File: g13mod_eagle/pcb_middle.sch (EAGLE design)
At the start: 65 parts

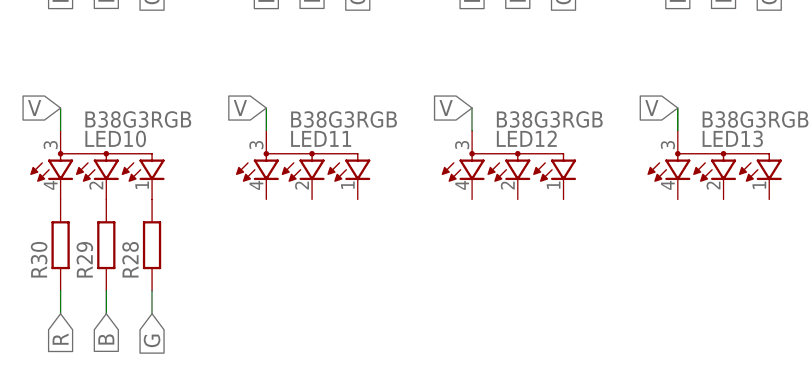
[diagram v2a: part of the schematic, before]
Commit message: wiring middle pcb
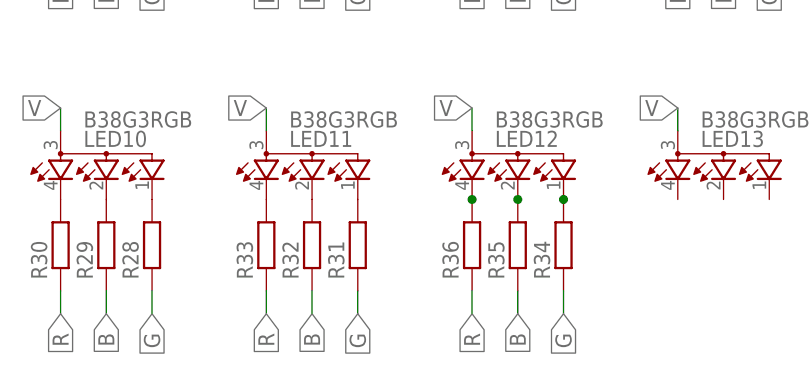
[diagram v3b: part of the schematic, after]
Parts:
- added R31, R32, R33, R34, R35, R36: (no value), rcl:R-EU_R0603
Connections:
- new net N$31: LED11.CGREEN, R31.2
- new net N$32: LED11.CBLUE, R32.2
- new net N$33: LED11.CRED, R33.2
- new net N$34: LED12.CGREEN, R34.2
- new net N$35: LED12.CBLUE, R35.2
- new net N$36: LED12.CRED, R36.2
- net B: now also R32.1, R35.1
- net G: now also R31.1, R34.1
- net R: now also R33.1, R36.1
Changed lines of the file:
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@@
 <part name="R29" library="rcl" library_urn="urn:adsk.eagle:library:334" deviceset="R-EU_" device="R0603" package3d_urn="urn:adsk.eagle:package:23555/3"/>
 <part name="R30" library="rcl" library_urn="urn:adsk.eagle:library:334" deviceset="R-EU_" device="R0603" package3d_urn="urn:adsk.eagle:package:23555/3"/>
+<part name="R31" library="rcl" library_urn="urn:adsk.eagle:library:334" deviceset="R-EU_" device="R0603" package3d_urn="urn:adsk.eagle:package:23555/3"/>
+<part name="R32" library="rcl" library_urn="urn:adsk.eagle:library:334" deviceset="R-EU_" device="R0603" package3d_urn="urn:adsk.eagle:package:23555/3"/>
+<part name="R33" library="rcl" library_urn="urn:adsk.eagle:library:334" deviceset="R-EU_" device="R0603" package3d_urn="urn:adsk.eagle:package:23555/3"/>
+<part name="R34" library="rcl" library_urn="urn:adsk.eagle:library:334" deviceset="R-EU_" device="R0603" package3d_urn="urn:adsk.eagle:package:23555/3"/>
+<part name="R35" library="rcl" library_urn="urn:adsk.eagle:library:334" deviceset="R-EU_" device="R0603" package3d_urn="urn:adsk.eagle:package:23555/3"/>
+<part name="R36" library="rcl" library_urn="urn:adsk.eagle:library:334" deviceset="R-EU_" device="R0603" package3d_urn="urn:adsk.eagle:package:23555/3"/>
 </parts>
 <sheets>
@@
 <attribute name="VALUE" x="66.802" y="-125.73" size="1.778" layer="96" rot="R90"/>
 </instance>
+<instance part="R31" gate="G$1" x="96.52" y="-121.92" smashed="yes" rot="R90">
+<attribute name="NAME" x="95.0214" y="-125.73" size="1.778" layer="95" rot="R90"/>
+<attribute name="VALUE" x="99.822" y="-125.73" size="1.778" layer="96" rot="R90"/>
+</instance>
+<instance part="R32" gate="G$1" x="91.44" y="-121.92" smashed="yes" rot="R90">
+<attribute name="NAME" x="89.9414" y="-125.73" size="1.778" layer="95" rot="R90"/>
+<attribute name="VALUE" x="94.742" y="-125.73" size="1.778" layer="96" rot="R90"/>
+</instance>
+<instance part="R33" gate="G$1" x="86.36" y="-121.92" smashed="yes" rot="R90">
+<attribute name="NAME" x="84.8614" y="-125.73" size="1.778" layer="95" rot="R90"/>
+<attribute name="VALUE" x="89.662" y="-125.73" size="1.778" layer="96" rot="R90"/>
+</instance>
+<instance part="R34" gate="G$1" x="119.38" y="-121.92" smashed="yes" rot="R90">
+<attribute name="NAME" x="117.8814" y="-125.73" size="1.778" layer="95" rot="R90"/>
+<attribute name="VALUE" x="122.682" y="-125.73" size="1.778" layer="96" rot="R90"/>
+</instance>
+<instance part="R35" gate="G$1" x="114.3" y="-121.92" smashed="yes" rot="R90">
+<attribute name="NAME" x="112.8014" y="-125.73" size="1.778" layer="95" rot="R90"/>
+<attribute name="VALUE" x="117.602" y="-125.73" size="1.778" layer="96" rot="R90"/>
+</instance>
+<instance part="R36" gate="G$1" x="109.22" y="-121.92" smashed="yes" rot="R90">
+<attribute name="NAME" x="107.7214" y="-125.73" size="1.778" layer="95" rot="R90"/>
+<attribute name="VALUE" x="112.522" y="-125.73" size="1.778" layer="96" rot="R90"/>
+</instance>
 </instances>
 <busses>
@@
 <label x="68.58" y="-129.54" size="1.778" layer="95" rot="R270" xref="yes"/>
 </segment>
+<segment>
+<pinref part="R32" gate="G$1" pin="1"/>
+<wire x1="91.44" y1="-127" x2="91.44" y2="-129.54" width="0.1524" layer="91"/>
+<label x="91.44" y="-129.54" size="1.778" layer="95" rot="R270" xref="yes"/>
+</segment>
+<segment>
+<pinref part="R35" gate="G$1" pin="1"/>
+<wire x1="114.3" y1="-127" x2="114.3" y2="-129.54" width="0.1524" layer="91"/>
+<label x="114.3" y="-129.54" size="1.778" layer="95" rot="R270" xref="yes"/>
+</segment>
 </net>
 <net name="R" class="0">
@@
 <label x="63.5" y="-129.54" size="1.778" layer="95" rot="R270" xref="yes"/>
 </segment>
+<segment>
+<pinref part="R33" gate="G$1" pin="1"/>
+<wire x1="86.36" y1="-127" x2="86.36" y2="-129.54" width="0.1524" layer="91"/>
+<label x="86.36" y="-129.54" size="1.778" layer="95" rot="R270" xref="yes"/>
+</segment>
+<segment>
+<pinref part="R36" gate="G$1" pin="1"/>
+<wire x1="109.22" y1="-127" x2="109.22" y2="-129.54" width="0.1524" layer="91"/>
+<label x="109.22" y="-129.54" size="1.778" layer="95" rot="R270" xref="yes"/>
+</segment>
 </net>
 <net name="G" class="0">
@@
 <wire x1="73.66" y1="-127" x2="73.66" y2="-129.54" width="0.1524" layer="91"/>
 <label x="73.66" y="-129.54" size="1.778" layer="95" rot="R270" xref="yes"/>
+</segment>
+<segment>
+<pinref part="R31" gate="G$1" pin="1"/>
+<wire x1="96.52" y1="-127" x2="96.52" y2="-129.54" width="0.1524" layer="91"/>
+<label x="96.52" y="-129.54" size="1.778" layer="95" rot="R270" xref="yes"/>
+</segment>
+<segment>
+<pinref part="R34" gate="G$1" pin="1"/>
+<wire x1="119.38" y1="-127" x2="119.38" y2="-129.54" width="0.1524" layer="91"/>
+<label x="119.38" y="-129.54" size="1.778" layer="95" rot="R270" xref="yes"/>
 </segment>
 </net>
@@
 </segment>
 </net>
+<net name="N$31" class="0">
+<segment>
+<pinref part="R31" gate="G$1" pin="2"/>
+<pinref part="LED11" gate="G$1" pin="CGREEN"/>
+</segment>
+</net>
+<net name="N$32" class="0">
+<segment>
+<pinref part="R32" gate="G$1" pin="2"/>
+<pinref part="LED11" gate="G$1" pin="CBLUE"/>
+</segment>
+</net>
+<net name="N$33" class="0">
+<segment>
+<pinref part="R33" gate="G$1" pin="2"/>
+<pinref part="LED11" gate="G$1" pin="CRED"/>
+</segment>
+</net>
+<net name="N$34" class="0">
+<segment>
+<pinref part="R34" gate="G$1" pin="2"/>
+<junction x="119.38" y="-116.84"/>
+<pinref part="LED12" gate="G$1" pin="CGREEN"/>
+</segment>
+</net>
+<net name="N$35" class="0">
+<segment>
+<pinref part="R35" gate="G$1" pin="2"/>
+<junction x="114.3" y="-116.84"/>
+<pinref part="LED12" gate="G$1" pin="CBLUE"/>
+</segment>
+</net>
+<net name="N$36" class="0">
+<segment>
+<pinref part="R36" gate="G$1" pin="2"/>
+<junction x="109.22" y="-116.84"/>
+<pinref part="LED12" gate="G$1" pin="CRED"/>
+</segment>
+</net>

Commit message: wiring middle pcb
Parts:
- added R37, R38, R39, R40, R41, R42, R43, R44, R45: (no value), rcl:R-EU_R0603
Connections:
- new net N$37: LED13.CGREEN, R37.2
- new net N$38: LED13.CBLUE, R38.2
- new net N$39: LED13.CRED, R39.2
- new net N$40: LED14.CGREEN, R40.2
- new net N$41: LED14.CBLUE, R41.2
- new net N$42: LED14.CRED, R42.2
- new net N$43: D1.BLUE_CATHODE, R43.2
- new net N$44: D1.GREEN_CATHODE, R44.2
- new net N$45: D1.RED_CATHODE, R45.2
- net B: now also R38.1, R41.1, R44.1
- net G: now also R37.1, R40.1, R43.1
- net R: now also R39.1, R42.1, R45.1
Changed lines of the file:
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@@
 <part name="R35" library="rcl" library_urn="urn:adsk.eagle:library:334" deviceset="R-EU_" device="R0603" package3d_urn="urn:adsk.eagle:package:23555/3"/>
 <part name="R36" library="rcl" library_urn="urn:adsk.eagle:library:334" deviceset="R-EU_" device="R0603" package3d_urn="urn:adsk.eagle:package:23555/3"/>
+<part name="R37" library="rcl" library_urn="urn:adsk.eagle:library:334" deviceset="R-EU_" device="R0603" package3d_urn="urn:adsk.eagle:package:23555/3"/>
+<part name="R38" library="rcl" library_urn="urn:adsk.eagle:library:334" deviceset="R-EU_" device="R0603" package3d_urn="urn:adsk.eagle:package:23555/3"/>
+<part name="R39" library="rcl" library_urn="urn:adsk.eagle:library:334" deviceset="R-EU_" device="R0603" package3d_urn="urn:adsk.eagle:package:23555/3"/>
+<part name="R40" library="rcl" library_urn="urn:adsk.eagle:library:334" deviceset="R-EU_" device="R0603" package3d_urn="urn:adsk.eagle:package:23555/3"/>
+<part name="R41" library="rcl" library_urn="urn:adsk.eagle:library:334" deviceset="R-EU_" device="R0603" package3d_urn="urn:adsk.eagle:package:23555/3"/>
+<part name="R42" library="rcl" library_urn="urn:adsk.eagle:library:334" deviceset="R-EU_" device="R0603" package3d_urn="urn:adsk.eagle:package:23555/3"/>
+<part name="R43" library="rcl" library_urn="urn:adsk.eagle:library:334" deviceset="R-EU_" device="R0603" package3d_urn="urn:adsk.eagle:package:23555/3"/>
+<part name="R44" library="rcl" library_urn="urn:adsk.eagle:library:334" deviceset="R-EU_" device="R0603" package3d_urn="urn:adsk.eagle:package:23555/3"/>
+<part name="R45" library="rcl" library_urn="urn:adsk.eagle:library:334" deviceset="R-EU_" device="R0603" package3d_urn="urn:adsk.eagle:package:23555/3"/>
 </parts>
 <sheets>
@@
 <attribute name="VALUE" x="112.522" y="-125.73" size="1.778" layer="96" rot="R90"/>
 </instance>
+<instance part="R37" gate="G$1" x="142.24" y="-121.92" smashed="yes" rot="R90">
+<attribute name="NAME" x="140.7414" y="-125.73" size="1.778" layer="95" rot="R90"/>
+<attribute name="VALUE" x="145.542" y="-125.73" size="1.778" layer="96" rot="R90"/>
+</instance>
+<instance part="R38" gate="G$1" x="137.16" y="-121.92" smashed="yes" rot="R90">
+<attribute name="NAME" x="135.6614" y="-125.73" size="1.778" layer="95" rot="R90"/>
+<attribute name="VALUE" x="140.462" y="-125.73" size="1.778" layer="96" rot="R90"/>
+</instance>
+<instance part="R39" gate="G$1" x="132.08" y="-121.92" smashed="yes" rot="R90">
+<attribute name="NAME" x="130.5814" y="-125.73" size="1.778" layer="95" rot="R90"/>
+<attribute name="VALUE" x="135.382" y="-125.73" size="1.778" layer="96" rot="R90"/>
+</instance>
+<instance part="R40" gate="G$1" x="165.1" y="-121.92" smashed="yes" rot="R90">
+<attribute name="NAME" x="163.6014" y="-125.73" size="1.778" layer="95" rot="R90"/>
+<attribute name="VALUE" x="168.402" y="-125.73" size="1.778" layer="96" rot="R90"/>
+</instance>
+<instance part="R41" gate="G$1" x="160.02" y="-121.92" smashed="yes" rot="R90">
+<attribute name="NAME" x="158.5214" y="-125.73" size="1.778" layer="95" rot="R90"/>
+<attribute name="VALUE" x="163.322" y="-125.73" size="1.778" layer="96" rot="R90"/>
+</instance>
+<instance part="R42" gate="G$1" x="154.94" y="-121.92" smashed="yes" rot="R90">
+<attribute name="NAME" x="153.4414" y="-125.73" size="1.778" layer="95" rot="R90"/>
+<attribute name="VALUE" x="158.242" y="-125.73" size="1.778" layer="96" rot="R90"/>
+</instance>
+<instance part="R43" gate="G$1" x="208.28" y="-73.66" smashed="yes" rot="R180">
+<attribute name="NAME" x="212.09" y="-75.1586" size="1.778" layer="95" rot="R180"/>
+<attribute name="VALUE" x="212.09" y="-70.358" size="1.778" layer="96" rot="R180"/>
+</instance>
+<instance part="R44" gate="G$1" x="208.28" y="-88.9" smashed="yes" rot="R180">
+<attribute name="NAME" x="212.09" y="-90.3986" size="1.778" layer="95" rot="R180"/>
+<attribute name="VALUE" x="212.09" y="-85.598" size="1.778" layer="96" rot="R180"/>
+</instance>
+<instance part="R45" gate="G$1" x="208.28" y="-81.28" smashed="yes" rot="R180">
+<attribute name="NAME" x="212.09" y="-82.7786" size="1.778" layer="95" rot="R180"/>
+<attribute name="VALUE" x="212.09" y="-77.978" size="1.778" layer="96" rot="R180"/>
+</instance>
 </instances>
 <busses>
@@
 <label x="114.3" y="-129.54" size="1.778" layer="95" rot="R270" xref="yes"/>
 </segment>
+<segment>
+<pinref part="R38" gate="G$1" pin="1"/>
+<wire x1="137.16" y1="-127" x2="137.16" y2="-129.54" width="0.1524" layer="91"/>
+<label x="137.16" y="-129.54" size="1.778" layer="95" rot="R270" xref="yes"/>
+</segment>
+<segment>
+<pinref part="R41" gate="G$1" pin="1"/>
+<wire x1="160.02" y1="-127" x2="160.02" y2="-129.54" width="0.1524" layer="91"/>
+<label x="160.02" y="-129.54" size="1.778" layer="95" rot="R270" xref="yes"/>
+</segment>
+<segment>
+<pinref part="R44" gate="G$1" pin="1"/>
+<wire x1="213.36" y1="-88.9" x2="215.9" y2="-88.9" width="0.1524" layer="91"/>
+<label x="215.9" y="-88.9" size="1.778" layer="95" xref="yes"/>
+</segment>
 </net>
 <net name="R" class="0">
@@
 <label x="109.22" y="-129.54" size="1.778" layer="95" rot="R270" xref="yes"/>
 </segment>
+<segment>
+<pinref part="R39" gate="G$1" pin="1"/>
+<wire x1="132.08" y1="-127" x2="132.08" y2="-129.54" width="0.1524" layer="91"/>
+<label x="132.08" y="-129.54" size="1.778" layer="95" rot="R270" xref="yes"/>
+</segment>
+<segment>
+<pinref part="R42" gate="G$1" pin="1"/>
+<wire x1="154.94" y1="-127" x2="154.94" y2="-129.54" width="0.1524" layer="91"/>
+<label x="154.94" y="-129.54" size="1.778" layer="95" rot="R270" xref="yes"/>
+</segment>
+<segment>
+<pinref part="R45" gate="G$1" pin="1"/>
+<wire x1="213.36" y1="-81.28" x2="215.9" y2="-81.28" width="0.1524" layer="91"/>
+<label x="215.9" y="-81.28" size="1.778" layer="95" xref="yes"/>
+</segment>
 </net>
 <net name="G" class="0">
@@
 <wire x1="119.38" y1="-127" x2="119.38" y2="-129.54" width="0.1524" layer="91"/>
 <label x="119.38" y="-129.54" size="1.778" layer="95" rot="R270" xref="yes"/>
+</segment>
+<segment>
+<pinref part="R37" gate="G$1" pin="1"/>
+<wire x1="142.24" y1="-127" x2="142.24" y2="-129.54" width="0.1524" layer="91"/>
+<label x="142.24" y="-129.54" size="1.778" layer="95" rot="R270" xref="yes"/>
+</segment>
+<segment>
+<pinref part="R40" gate="G$1" pin="1"/>
+<wire x1="165.1" y1="-127" x2="165.1" y2="-129.54" width="0.1524" layer="91"/>
+<label x="165.1" y="-129.54" size="1.778" layer="95" rot="R270" xref="yes"/>
+</segment>
+<segment>
+<pinref part="R43" gate="G$1" pin="1"/>
+<wire x1="213.36" y1="-73.66" x2="215.9" y2="-73.66" width="0.1524" layer="91"/>
+<label x="215.9" y="-73.66" size="1.778" layer="95" xref="yes"/>
 </segment>
 </net>
@@
 <segment>
 <pinref part="R4" gate="G$1" pin="2"/>
-<junction x="45.72" y="-78.74"/>
 <pinref part="LED2" gate="G$1" pin="CGREEN"/>
 </segment>
@@
 <segment>
 <pinref part="R5" gate="G$1" pin="2"/>
-<junction x="40.64" y="-78.74"/>
 <pinref part="LED2" gate="G$1" pin="CBLUE"/>
 </segment>
@@
 <segment>
 <pinref part="R6" gate="G$1" pin="2"/>
-<junction x="35.56" y="-78.74"/>
 <pinref part="LED2" gate="G$1" pin="CRED"/>
 </segment>
@@
 <segment>
 <pinref part="R7" gate="G$1" pin="2"/>
-<junction x="73.66" y="-78.74"/>
 <pinref part="LED3" gate="G$1" pin="CGREEN"/>
 </segment>
@@
 <segment>
 <pinref part="R8" gate="G$1" pin="2"/>
-<junction x="68.58" y="-78.74"/>
 <pinref part="LED3" gate="G$1" pin="CBLUE"/>
 </segment>
@@
 <segment>
 <pinref part="R9" gate="G$1" pin="2"/>
-<junction x="63.5" y="-78.74"/>
 <pinref part="LED3" gate="G$1" pin="CRED"/>
 </segment>
@@
 <segment>
 <pinref part="R10" gate="G$1" pin="2"/>
-<junction x="96.52" y="-78.74"/>
 <pinref part="LED4" gate="G$1" pin="CGREEN"/>
 </segment>
@@
 <segment>
 <pinref part="R11" gate="G$1" pin="2"/>
-<junction x="91.44" y="-78.74"/>
 <pinref part="LED4" gate="G$1" pin="CBLUE"/>
 </segment>
@@
 <segment>
 <pinref part="R12" gate="G$1" pin="2"/>
-<junction x="86.36" y="-78.74"/>
 <pinref part="LED4" gate="G$1" pin="CRED"/>
 </segment>
@@
 <segment>
 <pinref part="R13" gate="G$1" pin="2"/>
-<junction x="119.38" y="-78.74"/>
 <pinref part="LED5" gate="G$1" pin="CGREEN"/>
 </segment>
@@
 <segment>
 <pinref part="R14" gate="G$1" pin="2"/>
-<junction x="114.3" y="-78.74"/>
 <pinref part="LED5" gate="G$1" pin="CBLUE"/>
 </segment>
@@
 <segment>
 <pinref part="R15" gate="G$1" pin="2"/>
-<junction x="109.22" y="-78.74"/>
 <pinref part="LED5" gate="G$1" pin="CRED"/>
 </segment>
@@
 </segment>
 </net>
+<net name="N$37" class="0">
+<segment>
+<pinref part="R37" gate="G$1" pin="2"/>
+<pinref part="LED13" gate="G$1" pin="CGREEN"/>
+</segment>
+</net>
+<net name="N$38" class="0">
+<segment>
+<pinref part="R38" gate="G$1" pin="2"/>
+<pinref part="LED13" gate="G$1" pin="CBLUE"/>
+</segment>
+</net>
+<net name="N$39" class="0">
+<segment>
+<pinref part="R39" gate="G$1" pin="2"/>
+<pinref part="LED13" gate="G$1" pin="CRED"/>
+</segment>
+</net>
+<net name="N$40" class="0">
+<segment>
+<pinref part="R40" gate="G$1" pin="2"/>
+<pinref part="LED14" gate="G$1" pin="CGREEN"/>
+</segment>
+</net>
+<net name="N$41" class="0">
+<segment>
+<pinref part="R41" gate="G$1" pin="2"/>
+<pinref part="LED14" gate="G$1" pin="CBLUE"/>
+</segment>
+</net>
+<net name="N$42" class="0">
+<segment>
+<pinref part="R42" gate="G$1" pin="2"/>
+<pinref part="LED14" gate="G$1" pin="CRED"/>
+</segment>
+</net>
+<net name="N$43" class="0">
+<segment>
+<pinref part="R43" gate="G$1" pin="2"/>
+<pinref part="D1" gate="G$1" pin="BLUE_CATHODE"/>
+</segment>
+</net>
+<net name="N$44" class="0">
+<segment>
+<pinref part="R44" gate="G$1" pin="2"/>
+<pinref part="D1" gate="G$1" pin="GREEN_CATHODE"/>
+</segment>
+</net>
+<net name="N$45" class="0">
+<segment>
+<pinref part="R45" gate="G$1" pin="2"/>
+<pinref part="D1" gate="G$1" pin="RED_CATHODE"/>
+</segment>
+</net>

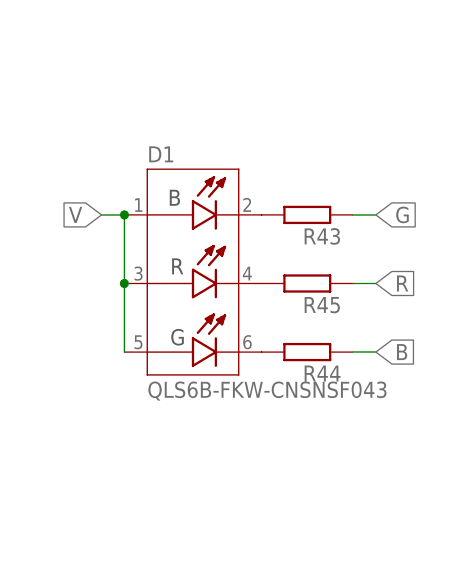
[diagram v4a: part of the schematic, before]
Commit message: Fix LED color
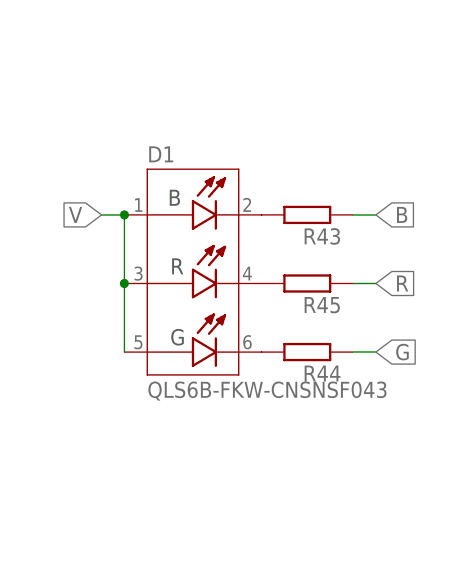
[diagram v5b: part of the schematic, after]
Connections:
- net B: now also R43.1; no longer R44.1
- net G: now also R44.1; no longer R43.1
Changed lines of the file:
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@@
 </segment>
 <segment>
-<pinref part="R44" gate="G$1" pin="1"/>
-<wire x1="213.36" y1="-88.9" x2="215.9" y2="-88.9" width="0.1524" layer="91"/>
-<label x="215.9" y="-88.9" size="1.778" layer="95" xref="yes"/>
+<pinref part="R43" gate="G$1" pin="1"/>
+<wire x1="213.36" y1="-73.66" x2="215.9" y2="-73.66" width="0.1524" layer="91"/>
+<label x="215.9" y="-73.66" size="1.778" layer="95" xref="yes"/>
 </segment>
 </net>
@@
 </segment>
 <segment>
-<pinref part="R43" gate="G$1" pin="1"/>
-<wire x1="213.36" y1="-73.66" x2="215.9" y2="-73.66" width="0.1524" layer="91"/>
-<label x="215.9" y="-73.66" size="1.778" layer="95" xref="yes"/>
+<pinref part="R44" gate="G$1" pin="1"/>
+<wire x1="213.36" y1="-88.9" x2="215.9" y2="-88.9" width="0.1524" layer="91"/>
+<label x="215.9" y="-88.9" size="1.778" layer="95" xref="yes"/>
 </segment>
 </net>
